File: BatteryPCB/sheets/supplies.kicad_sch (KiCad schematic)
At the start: 6 parts, among them J5 to COTS altimeter, J6 to SRAD flight computer, SW2 COTS ARM, SW3 SRAD ARM

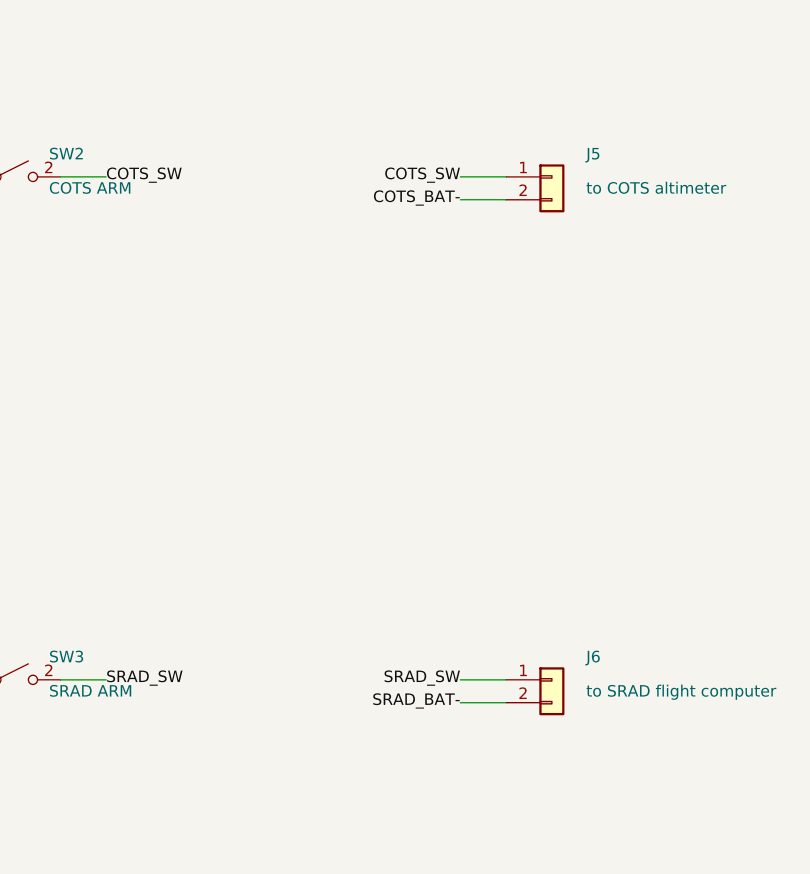
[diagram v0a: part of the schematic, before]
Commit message: Battery PCB v18: antenna clearance, stack outline, cut-outs, XT30 outputs
Second design review:
- ESP32 antenna: back-copper keep-out (no pour, tracks or vias) 15 mm to
  each side of and past the DevKitC antenna, outlined on the back silk;
  COTS_SW rerouted around it; nylon M3 note for H5, the stack bolt over it.
- Pin-switch stack outlined on the front silk.
- Two spare 12 x 7 mm wire pass-throughs at the upper left.
- J5/J6 battery outputs are AMASS XT30UPB-F (pin 1 minus, pin 2 plus);
  schematic labels swapped to match, BOM and cable-side parts updated.
ERC 0 errors, DRC 0 (strict, schematic parity), verify_A all pass.

Co-Authored-By: Claude Opus 5.5 <noreply@anthropic.com>
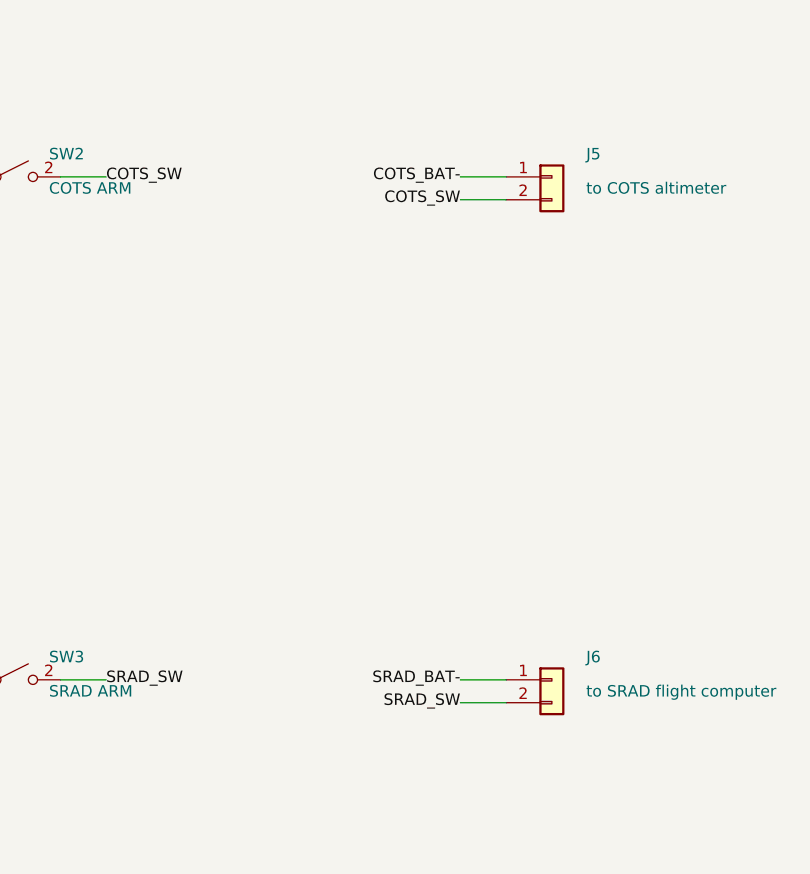
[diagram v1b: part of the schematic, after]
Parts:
- J5: footprint battery_pcb:Molex_Micro-Fit_3.0_43650-0215_1x02_P3.00mm_Vertical -> battery_pcb:AMASS_XT30UPB-F_1x02_P5.0mm_Vertical; MPN 0436500215 -> XT30UPB-F; Manufacturer Molex -> AMASS
- J6: footprint Connector_JST:JST_XH_B2B-XH-A_1x02_P2.50mm_Vertical -> battery_pcb:AMASS_XT30UPB-F_1x02_P5.0mm_Vertical; MPN B2B-XH-A(LF)(SN) -> XT30UPB-F; Manufacturer JST -> AMASS
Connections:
- net COTS_BAT-: now also J5.1 (Pin_1); no longer J5.2 (Pin_2)
- net COTS_SW: now also J5.2 (Pin_2); no longer J5.1 (Pin_1)
- net SRAD_BAT-: now also J6.1 (Pin_1); no longer J6.2 (Pin_2)
- net SRAD_SW: now also J6.2 (Pin_2); no longer J6.1 (Pin_1)
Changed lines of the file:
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@@
 			(effects (font (size 1.27 1.27)) (justify left))
 		)
-		(property "Footprint" "battery_pcb:Molex_Micro-Fit_3.0_43650-0215_1x02_P3.00mm_Vertical"
-			(at 154.94 54.61 0)
-			(effects (font (size 1.27 1.27)) (hide yes))
-		)
-		(property "Datasheet" ""
-			(at 154.94 54.61 0)
-			(effects (font (size 1.27 1.27)) (hide yes))
-		)
-		(property "Manufacturer" "Molex"
-			(at 154.94 54.61 0)
-			(effects (font (size 1.27 1.27)) (hide yes))
-		)
-		(property "MPN" "0436500215"
+		(property "Footprint" "battery_pcb:AMASS_XT30UPB-F_1x02_P5.0mm_Vertical"
+			(at 154.94 54.61 0)
+			(effects (font (size 1.27 1.27)) (hide yes))
+		)
+		(property "Datasheet" ""
+			(at 154.94 54.61 0)
+			(effects (font (size 1.27 1.27)) (hide yes))
+		)
+		(property "Manufacturer" "AMASS"
+			(at 154.94 54.61 0)
+			(effects (font (size 1.27 1.27)) (hide yes))
+		)
+		(property "MPN" "XT30UPB-F"
 			(at 154.94 54.61 0)
 			(effects (font (size 1.27 1.27)) (hide yes))
@@
 		(stroke (width 0) (type default))
 	)
+	(label "COTS_BAT-"
+		(at 144.78 54.61 180)
+		(fields_autoplaced yes)
+		(effects (font (size 1.27 1.27)) (justify right))
+	)
+	(wire
+		(pts (xy 149.86 57.15) (xy 144.78 57.15))
+		(stroke (width 0) (type default))
+	)
 	(label "COTS_SW"
-		(at 144.78 54.61 180)
-		(fields_autoplaced yes)
-		(effects (font (size 1.27 1.27)) (justify right))
-	)
-	(wire
-		(pts (xy 149.86 57.15) (xy 144.78 57.15))
-		(stroke (width 0) (type default))
-	)
-	(label "COTS_BAT-"
 		(at 144.78 57.15 180)
 		(fields_autoplaced yes)
@@
 			(effects (font (size 1.27 1.27)) (justify left))
 		)
-		(property "Footprint" "Connector_JST:JST_XH_B2B-XH-A_1x02_P2.50mm_Vertical"
-			(at 154.94 110.49 0)
-			(effects (font (size 1.27 1.27)) (hide yes))
-		)
-		(property "Datasheet" ""
-			(at 154.94 110.49 0)
-			(effects (font (size 1.27 1.27)) (hide yes))
-		)
-		(property "Manufacturer" "JST"
-			(at 154.94 110.49 0)
-			(effects (font (size 1.27 1.27)) (hide yes))
-		)
-		(property "MPN" "B2B-XH-A(LF)(SN)"
+		(property "Footprint" "battery_pcb:AMASS_XT30UPB-F_1x02_P5.0mm_Vertical"
+			(at 154.94 110.49 0)
+			(effects (font (size 1.27 1.27)) (hide yes))
+		)
+		(property "Datasheet" ""
+			(at 154.94 110.49 0)
+			(effects (font (size 1.27 1.27)) (hide yes))
+		)
+		(property "Manufacturer" "AMASS"
+			(at 154.94 110.49 0)
+			(effects (font (size 1.27 1.27)) (hide yes))
+		)
+		(property "MPN" "XT30UPB-F"
 			(at 154.94 110.49 0)
 			(effects (font (size 1.27 1.27)) (hide yes))
@@
 		(stroke (width 0) (type default))
 	)
+	(label "SRAD_BAT-"
+		(at 144.78 110.49 180)
+		(fields_autoplaced yes)
+		(effects (font (size 1.27 1.27)) (justify right))
+	)
+	(wire
+		(pts (xy 149.86 113.03) (xy 144.78 113.03))
+		(stroke (width 0) (type default))
+	)
 	(label "SRAD_SW"
-		(at 144.78 110.49 180)
-		(fields_autoplaced yes)
-		(effects (font (size 1.27 1.27)) (justify right))
-	)
-	(wire
-		(pts (xy 149.86 113.03) (xy 144.78 113.03))
-		(stroke (width 0) (type default))
-	)
-	(label "SRAD_BAT-"
 		(at 144.78 113.03 180)
 		(fields_autoplaced yes)
